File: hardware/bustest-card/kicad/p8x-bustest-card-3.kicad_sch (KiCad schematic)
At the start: 31 parts

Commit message: feat(sch): draw every P8X card schematic by function
Extend the functional-sheet grouping from the io-card to the control,
regbank, alu, memory, cf, ps2 and bustest cards. functional_sheets now
attaches unnamed glue gates, LEDs, resistors and connectors to the block
they share the most local nets with, so each block lists only its main
parts. A net with two or more pins on a sheet is now wired there even if
it continues elsewhere (its global name label rides on the wire), and
every wire is oriented by drawing side. The regbank gets one pointer per
sheet; the ps2 latches share a sheet with the AVR so the mailbox bus is
drawn. The bustest probe resistors use a straight-order RNISO8DSTR
drawing (the reversed B side forced every wire to cross and the sheet
fell back to labels). build_sch.sh now shows ELK fallbacks and clears old
numbered sheets before a build. All eight netlists match the boards,
ERC 0 errors; the boards change only in footprint link paths.

Co-Authored-By: Claude Opus 5.5 <noreply@anthropic.com>
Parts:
- removed C1, C2, C3, C4, C5, C6, C7: 100nF, Capacitor_THT:C_Disc_D5.0mm_W2.5mm_P5.00mm, symbol p8x:CAP1
- removed D1: SCHOTTKY, LED_THT:LED_D5.0mm, symbol p8x:LED
- removed LED10: ARM, LED_THT:LED_D5.0mm, symbol p8x:LED
- removed LED11: LIS, LED_THT:LED_D5.0mm, symbol p8x:LED
- removed LED12: CLK, LED_THT:LED_D5.0mm, symbol p8x:LED
- removed LED13: CKB, LED_THT:LED_D5.0mm, symbol p8x:LED
- removed LED14: RES, LED_THT:LED_D5.0mm, symbol p8x:LED
- removed LED15: ERR, LED_THT:LED_D5.0mm, symbol p8x:LED
- removed LED16: USB, LED_THT:LED_D5.0mm, symbol p8x:LED
- removed LED9: 5V, LED_THT:LED_D5.0mm, symbol p8x:LED
- removed R5, R6: 10K, Resistor_THT:R_Axial_DIN0207_L6.3mm_D2.5mm_P10.16mm_Horizontal, symbol p8x:RES
- removed R7: 1K8, Resistor_THT:R_Axial_DIN0207_L6.3mm_D2.5mm_P10.16mm_Horizontal, symbol p8x:RES
- removed R8: 3K3, Resistor_THT:R_Axial_DIN0207_L6.3mm_D2.5mm_P10.16mm_Horizontal, symbol p8x:RES
- removed RN2: 8x330R, Package_DIP:DIP-16_W7.62mm, symbol p8x:RNISO8D
- added J2: PROBE, Connector_PinHeader_2.54mm:PinHeader_1x10_P2.54mm_Vertical, symbol p8x:HDR10
- added U5: MCP23S17, Package_DIP:DIP-28_W7.62mm, symbol p8x:MCP23S17
- added U7: 74HCT244, Package_DIP:DIP-20_W7.62mm, symbol p8x:74244
- RN3: symbol p8x:RNISO8D -> p8x:RNISO8DSTR
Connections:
- net GND: now also J2.10, J2.9, U5.10, U5.15 (A0), U5.16 (A1), U5.19 (!INTB), U5.20 (!INTA), U7.1 (!G1), U7.10, U7.19 (!G2)
- net L_PR0: now also U7.18 (Y1)
- net L_PR1: now also U7.16 (Y2)
- net L_PR2: now also U7.14 (Y3)
- net L_PR3: now also U7.12 (Y4)
- net L_PR4: now also U7.9 (Y5)
- net L_PR5: now also U7.7 (Y6)
- net L_PR6: now also U7.5 (Y7)
- net L_PR7: now also U7.3 (Y8)
- net PR0: now also U5.21 (GPA0), U7.2 (A1)
- net PR1: now also U5.22 (GPA1), U7.4 (A2)
- net PR2: now also U5.23 (GPA2), U7.6 (A3)
- net PR3: now also U5.24 (GPA3), U7.8 (A4)
- net PR4: now also U5.25 (GPA4), U7.11 (A5)
- net PR5: now also U5.26 (GPA5), U7.13 (A6)
- net PR6: now also U5.27 (GPA6), U7.15 (A7)
- net PR7: now also U5.28 (GPA7), U7.17 (A8)
- net PRJ0: now also J2.1
- net PRJ1: now also J2.2
- net PRJ2: now also J2.3
- net PRJ3: now also J2.4
- net PRJ4: now also J2.5
- net PRJ5: now also J2.6
- net PRJ6: now also J2.7
- net PRJ7: now also J2.8
- net SO5: now also U5.14 (SO)
- net VCC: now also U5.17 (A2), U5.9, U7.20
- new net CS5: U5.11 (!CS)
- new net RST5: U5.18 (!RESET)
- new net SCK5: U5.12 (SCK)
- new net SI5: U5.13 (SI)
- new net SPARE12: U5.1 (GPB0)
- new net SPARE13: U5.2 (GPB1)
- new net SPARE14: U5.3 (GPB2)
- new net SPARE15: U5.4 (GPB3)
- new net SPARE16: U5.5 (GPB4)
- new net SPARE17: U5.6 (GPB5)
- no-connect marks 0 -> 2
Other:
- moved on the sheet: LED1, LED2, LED3, LED4, LED5, LED6, LED7, LED8, RN1, RN3

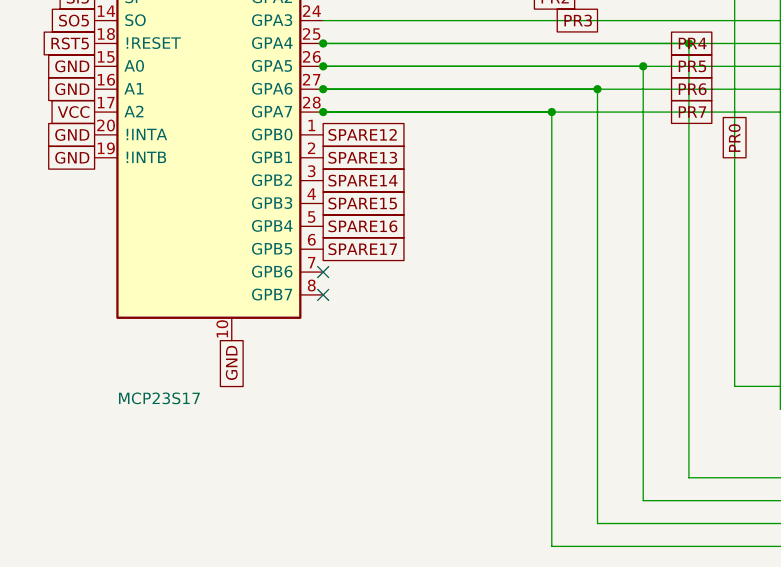
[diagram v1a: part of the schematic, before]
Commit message: fix(bustest): join IRQ and SPARE12-19 to the bus connector
The schematic ERC flagged single-pin labels on the bus test card: U4.GPA6
was named -IRQ while the bus line on B29 is IRQ, and the card's used_bus
set excluded every SPARE* net, so both allocations floated on the routed
board. Name the pin IRQ and map U5 port B to SPARE12-19 (B4-B18, the
design doc's allocation; was SPARE12-17), add the SPARE field to the
firmware table, and re-route the board: DRC 0 unconnected, PASS;
schematic ERC 0 errors, 0 warnings.

Co-Authored-By: Claude Opus 5.5 <noreply@anthropic.com>
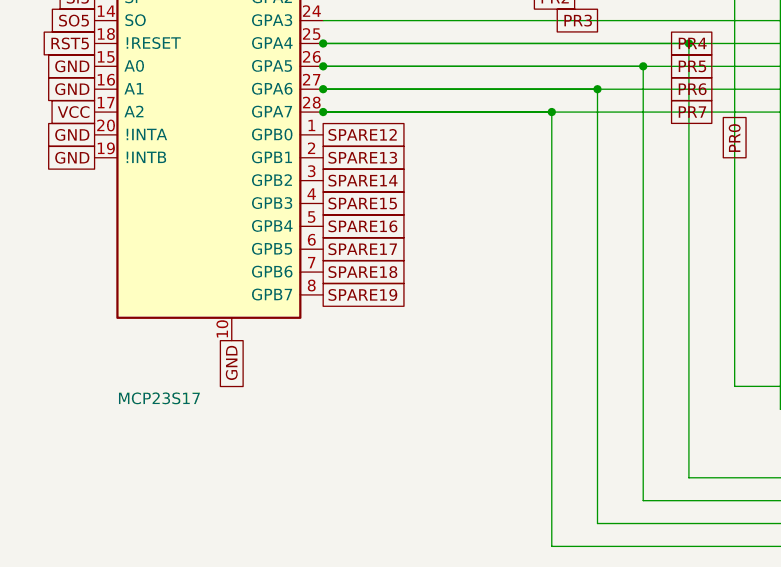
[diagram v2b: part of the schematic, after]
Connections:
- net SPARE18: now reaches U5.7 (GPB6)
- net SPARE19: now reaches U5.8 (GPB7)
- no-connect marks 2 -> 0
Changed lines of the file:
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@@
   (global_label "SPARE17" (shape passive) (at 86.36 172.72 0) (fields_autoplaced yes) (effects (font (size 1.27 1.27)) (justify left))
     (property "Intersheetrefs" "${INTERSHEET_REFS}" (at 86.36 172.72 0) (effects (font (size 1.27 1.27)) hide)))
-  (no_connect (at 86.36 175.26))
-  (no_connect (at 86.36 177.80))
+  (global_label "SPARE18" (shape passive) (at 86.36 175.26 0) (fields_autoplaced yes) (effects (font (size 1.27 1.27)) (justify left))
+    (property "Intersheetrefs" "${INTERSHEET_REFS}" (at 86.36 175.26 0) (effects (font (size 1.27 1.27)) hide)))
+  (global_label "SPARE19" (shape passive) (at 86.36 177.80 0) (fields_autoplaced yes) (effects (font (size 1.27 1.27)) (justify left))
+    (property "Intersheetrefs" "${INTERSHEET_REFS}" (at 86.36 177.80 0) (effects (font (size 1.27 1.27)) hide)))
   (global_label "VCC" (shape passive) (at 71.12 134.62 90) (fields_autoplaced yes) (effects (font (size 1.27 1.27)) (justify left))
     (property "Intersheetrefs" "${INTERSHEET_REFS}" (at 71.12 134.62 0) (effects (font (size 1.27 1.27)) hide)))
